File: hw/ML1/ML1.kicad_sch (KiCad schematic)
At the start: 7 parts, among them J1 Conn_01x06, J2 5-12V Supply, J4 Conn_01x02

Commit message: Re-work of ML1 board in process
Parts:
- removed J4: Conn_01x02, Connector_PinHeader_2.54mm:PinHeader_1x02_P2.54mm_Vertical, symbol Connector_Generic:Conn_01x02
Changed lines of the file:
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@@
-    (stroke (width 0) (type default))
-  )
-  (wire (pts (xy 205.74 100.33) (xy 218.44 100.33))
     (stroke (width 0) (type default))
   )
@@
     )
   )
-  (global_label "GPIO_PWR" (shape input) (at 205.74 100.33 180) (fields_autoplaced)
-    (effects (font (size 1.27 1.27)) (justify right))
-    (property "Intersheetrefs" "${INTERSHEET_REFS}" (at 193.3205 100.33 0)
-      (effects (font (size 1.27 1.27)) (justify right) hide)
-    )
-  )
   (global_label "RIG_AF_IN" (shape input) (at 226.06 77.47 0) (fields_autoplaced)
     (effects (font (size 1.27 1.27)) (justify left))
@@
         )
       )
-    )
-  )
-  (symbol (lib_id "Connector_Generic:Conn_01x02") (at 223.52 100.33 0) (unit 1)
-    (in_bom yes) (on_board yes) (dnp no) (fields_autoplaced)
-    (property "Reference" "J4" (at 226.06 100.33 0)
-      (effects (font (size 1.27 1.27)) (justify left))
-    )
-    (property "Value" "Conn_01x02" (at 226.06 102.87 0)
-      (effects (font (size 1.27 1.27)) (justify left))
-    )
-    (property "Footprint" "Connector_PinHeader_2.54mm:PinHeader_1x02_P2.54mm_Vertical" (at 223.52 100.33 0)
-      (effects (font (size 1.27 1.27)) hide)
-    )
-    (property "Datasheet" "~" (at 223.52 100.33 0)
-      (effects (font (size 1.27 1.27)) hide)
-    )
-    (pin "1")
-    (pin "2")
-    (instances
-      (project "ML1"
-        (path "/5f8f636b-fd0e-498e-8696-0a023acb4c09"
-          (reference "J4") (unit 1)
-        )
-      )
-    )
-  )
-  (symbol (lib_id "power:GNDA") (at 218.44 102.87 0) (unit 1)
-    (in_bom yes) (on_board yes) (dnp no) (fields_autoplaced)
-    (property "Reference" "#PWR028" (at 218.44 109.22 0)
-      (effects (font (size 1.27 1.27)) hide)
-    )
-    (property "Value" "GNDA" (at 218.44 107.95 0)
-      (effects (font (size 1.27 1.27)))
-    )
-    (property "Footprint" "" (at 218.44 102.87 0)
-      (effects (font (size 1.27 1.27)) hide)
-    )
-    (property "Datasheet" "" (at 218.44 102.87 0)
-      (effects (font (size 1.27 1.27)) hide)
-    )
-    (pin "1")
-    (instances
-      (project "ML1"
-        (path "/5f8f636b-fd0e-498e-8696-0a023acb4c09"
-          (reference "#PWR028") (unit 1)
-        )
-      )

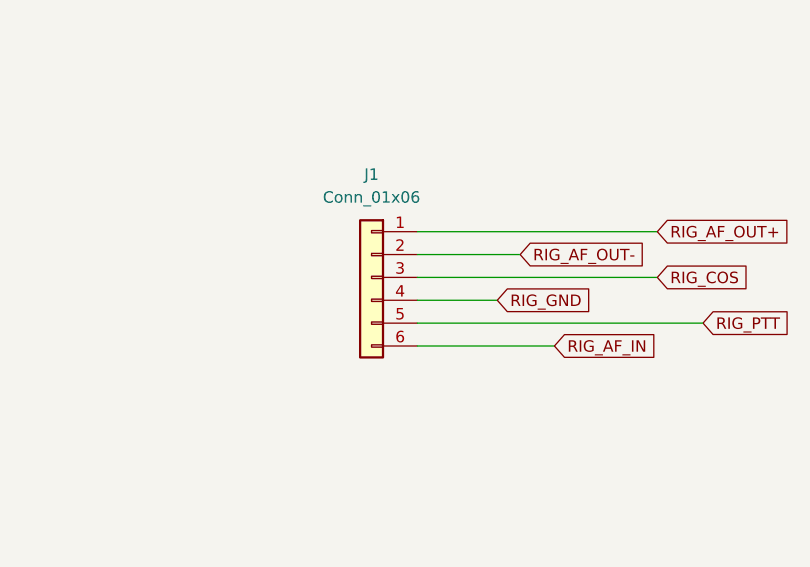
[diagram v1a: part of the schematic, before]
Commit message: Re-work of ML1 board in process
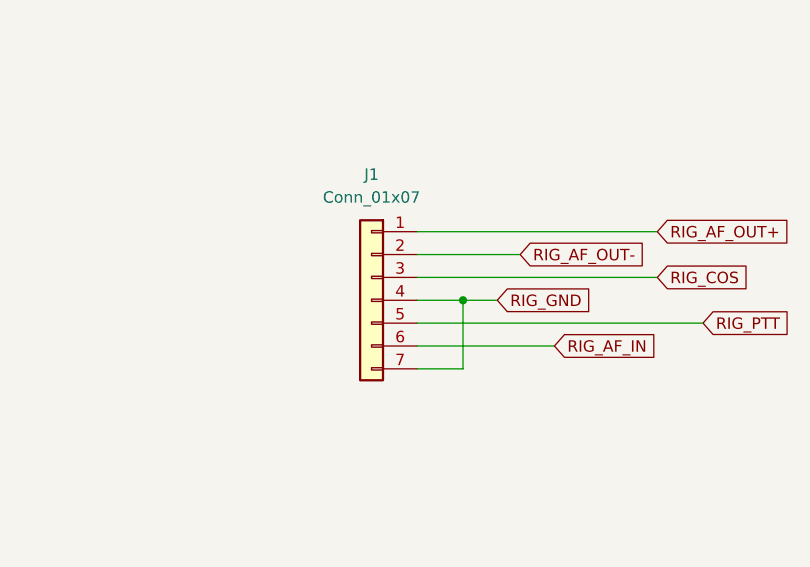
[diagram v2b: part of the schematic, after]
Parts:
- removed J1: Conn_01x06, Connector_PinHeader_2.54mm:PinHeader_1x06_P2.54mm_Vertical, symbol Connector_Generic:Conn_01x06
- added J1: Conn_01x07, Connector_PinHeader_2.54mm:PinHeader_1x07_P2.54mm_Vertical, symbol Connector_Generic:Conn_01x07
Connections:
- net RIG_AF_IN: now also J1.6 (Pin_6)
- net RIG_AF_OUT+: now also J1.1 (Pin_1)
- net RIG_AF_OUT-: now also J1.2 (Pin_2)
- net RIG_COS: now also J1.3 (Pin_3)
- net RIG_GND: now also J1.4 (Pin_4), J1.7 (Pin_7)
- net RIG_PTT: now also J1.5 (Pin_5)
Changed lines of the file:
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@@
     (comment 1 "Copyright (C) 2024 - Not For Commercial Use")
   )
+  (junction (at 215.9 72.39) (diameter 0) (color 0 0 0 0)
+  )
   (wire (pts (xy 210.82 69.85) (xy 237.49 69.85))
     (stroke (width 0) (type default))
@@
     (stroke (width 0) (type default))
   )
+  (wire (pts (xy 215.9 80.01) (xy 215.9 72.39))
+    (stroke (width 0) (type default))
+  )
   (wire (pts (xy 217.17 137.16) (xy 222.25 137.16))
     (stroke (width 0) (type default))
   )
+  (wire (pts (xy 210.82 80.01) (xy 215.9 80.01))
+    (stroke (width 0) (type default))
+  )
   (wire (pts (xy 222.25 137.16) (xy 222.25 132.08))
     (stroke (width 0) (type default))
@@
     (stroke (width 0) (type default))
   )
-  (wire (pts (xy 210.82 72.39) (xy 219.71 72.39))
+  (wire (pts (xy 215.9 72.39) (xy 219.71 72.39))
+    (stroke (width 0) (type default))
+  )
+  (wire (pts (xy 210.82 72.39) (xy 215.9 72.39))
     (stroke (width 0) (type default))
   )
@@
     )
   )
-  (symbol (lib_id "Connector_Generic:Conn_01x06") (at 205.74 69.85 0) (mirror y) (unit 1)
+  (symbol (lib_id "Connector_Generic:Conn_01x07") (at 205.74 72.39 0) (mirror y) (unit 1)
     (in_bom yes) (on_board yes) (dnp no) (fields_autoplaced)
     (property "Reference" "J1" (at 205.74 58.42 0)
       (effects (font (size 1.27 1.27)))
     )
-    (property "Value" "Conn_01x06" (at 205.74 60.96 0)
-      (effects (font (size 1.27 1.27)))
-    )
-    (property "Footprint" "Connector_PinHeader_2.54mm:PinHeader_1x06_P2.54mm_Vertical" (at 205.74 69.85 0)
-      (effects (font (size 1.27 1.27)) hide)
-    )
-    (property "Datasheet" "~" (at 205.74 69.85 0)
-      (effects (font (size 1.27 1.27)) hide)
-    )
+    (property "Value" "Conn_01x07" (at 205.74 60.96 0)
+      (effects (font (size 1.27 1.27)))
+    )
+    (property "Footprint" "Connector_PinHeader_2.54mm:PinHeader_1x07_P2.54mm_Vertical" (at 205.74 72.39 0)
+      (effects (font (size 1.27 1.27)) hide)
+    )
+    (property "Datasheet" "~" (at 205.74 72.39 0)
+      (effects (font (size 1.27 1.27)) hide)
+    )
+    (pin "6")
+    (pin "5")
+    (pin "7")
+    (pin "1")
+    (pin "4")
+    (pin "2")
     (pin "3")
-    (pin "2")
-    (pin "1")
-    (pin "5")
-    (pin "4")
-    (pin "6")
-    (instances
-      (project "ML1"
+    (instances
+      (project "ML1"
